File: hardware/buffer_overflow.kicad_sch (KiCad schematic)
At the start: 24 parts, among them J1 Upper Connector, J2 Lower Connector, U1 LM741

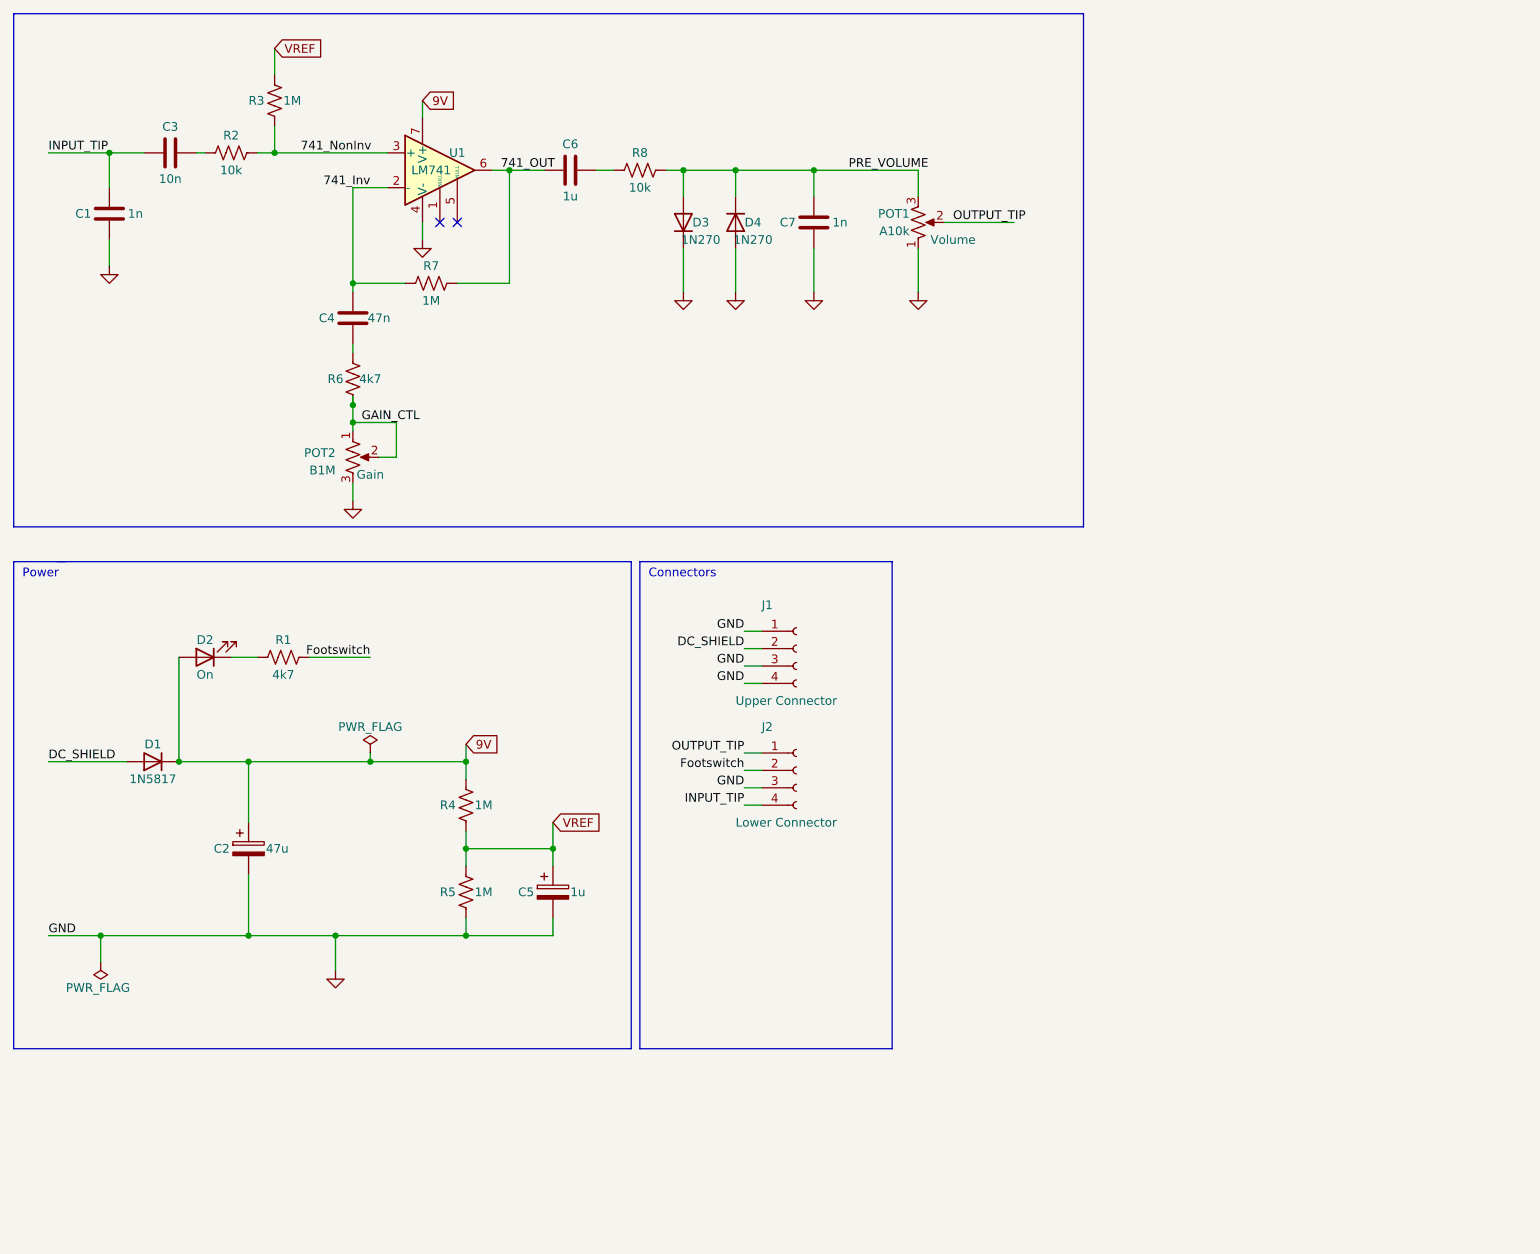
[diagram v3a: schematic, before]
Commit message: Offload functions of "noise floor" interface boards for v0.35
 - more layout changes coming, but functionality should be the same.
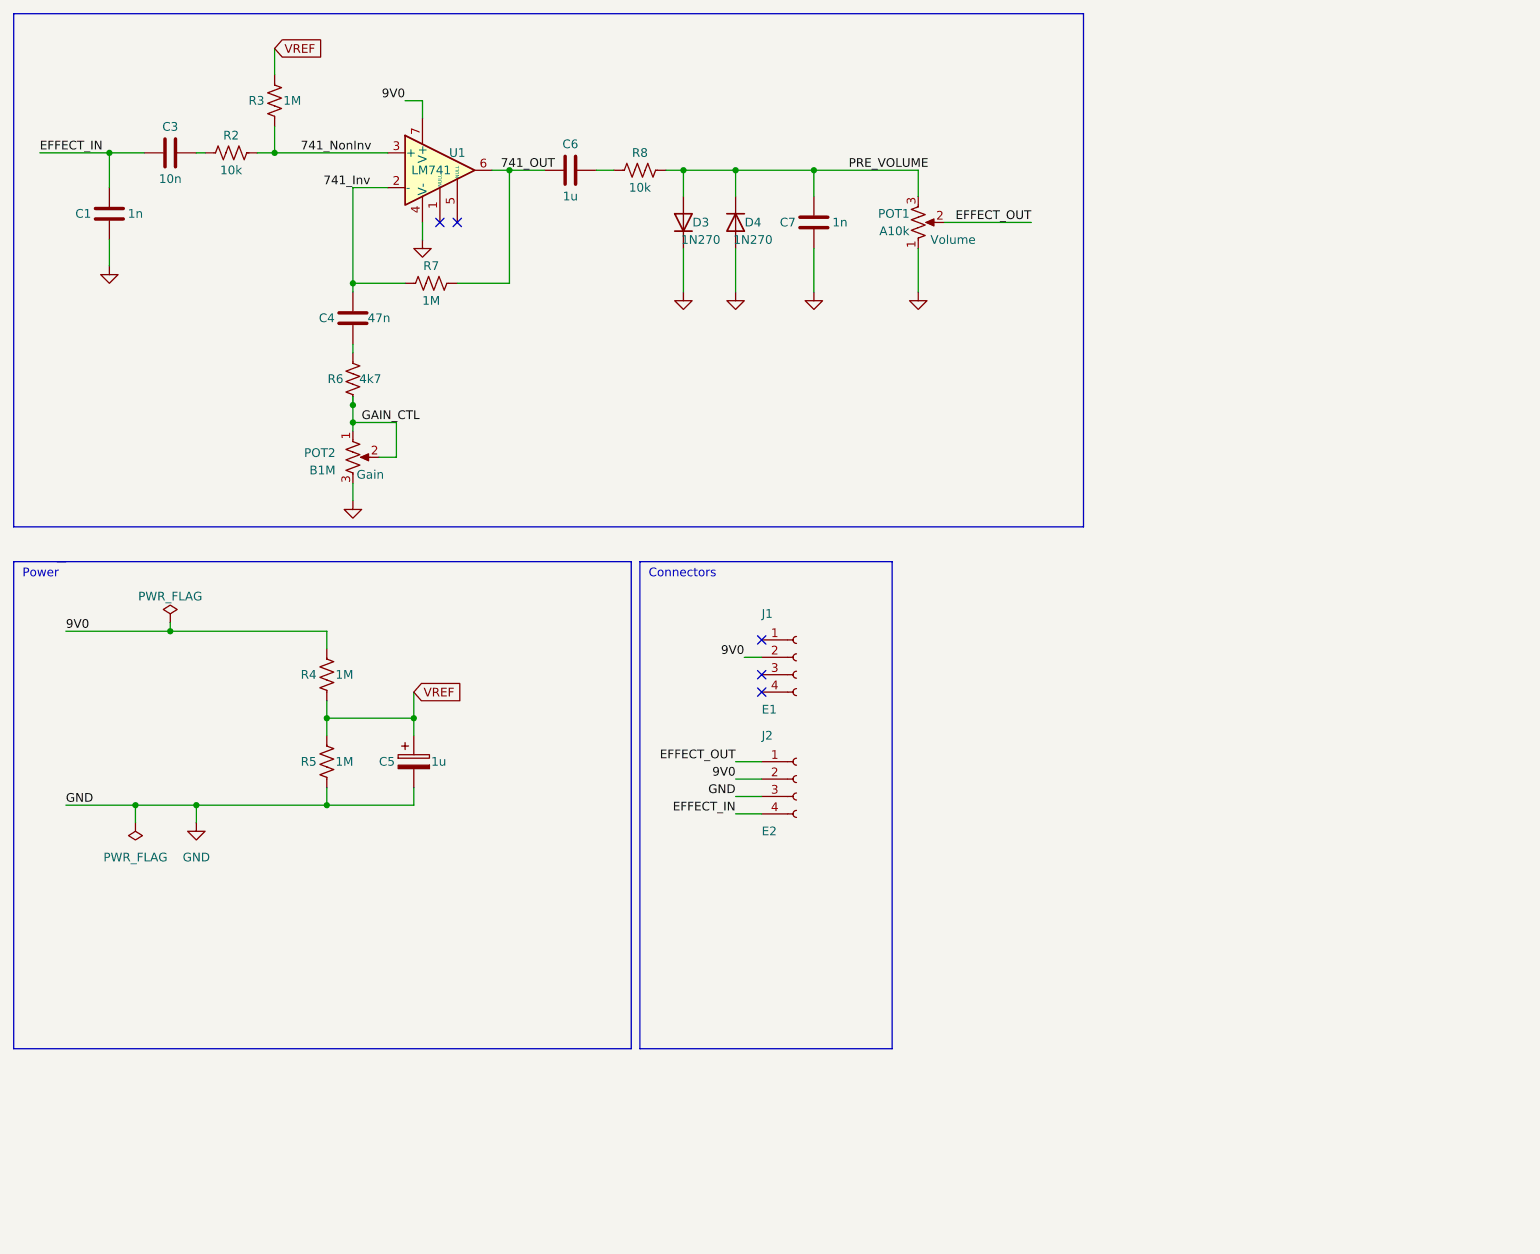
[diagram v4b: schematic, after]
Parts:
- removed C2: 47u, Capacitor_THT:CP_Radial_D5.0mm_P2.50mm, symbol Device:C_Polarized
- removed D1: 1N5817, Diode_THT:D_DO-35_SOD27_P7.62mm_Horizontal, symbol Device:D
- removed D2: On, LED_THT:LED_D3.0mm, symbol Device:LED
- removed R1: 4k7, Resistor_THT:R_Axial_DIN0207_L6.3mm_D2.5mm_P7.62mm_Horizontal, symbol Device:R_US
- J1: value Upper Connector -> E1
- J2: value Lower Connector -> E2
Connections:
- net DC_SHIELD is gone; now on net 9V0: J1.2 (Pin_2)
- net Footswitch is gone; now on net 9V0: J2.2 (Pin_2)
- net GND: no longer J1.1 (Pin_1), J1.3 (Pin_3), J1.4 (Pin_4)
- net 9V renamed 9V0
- net INPUT_TIP renamed EFFECT_IN
- net OUTPUT_TIP renamed EFFECT_OUT
- no-connect marks 2 -> 5
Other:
- moved on the sheet: C5, R4, R5

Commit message: condense to a single connector, bump rev to v0.38
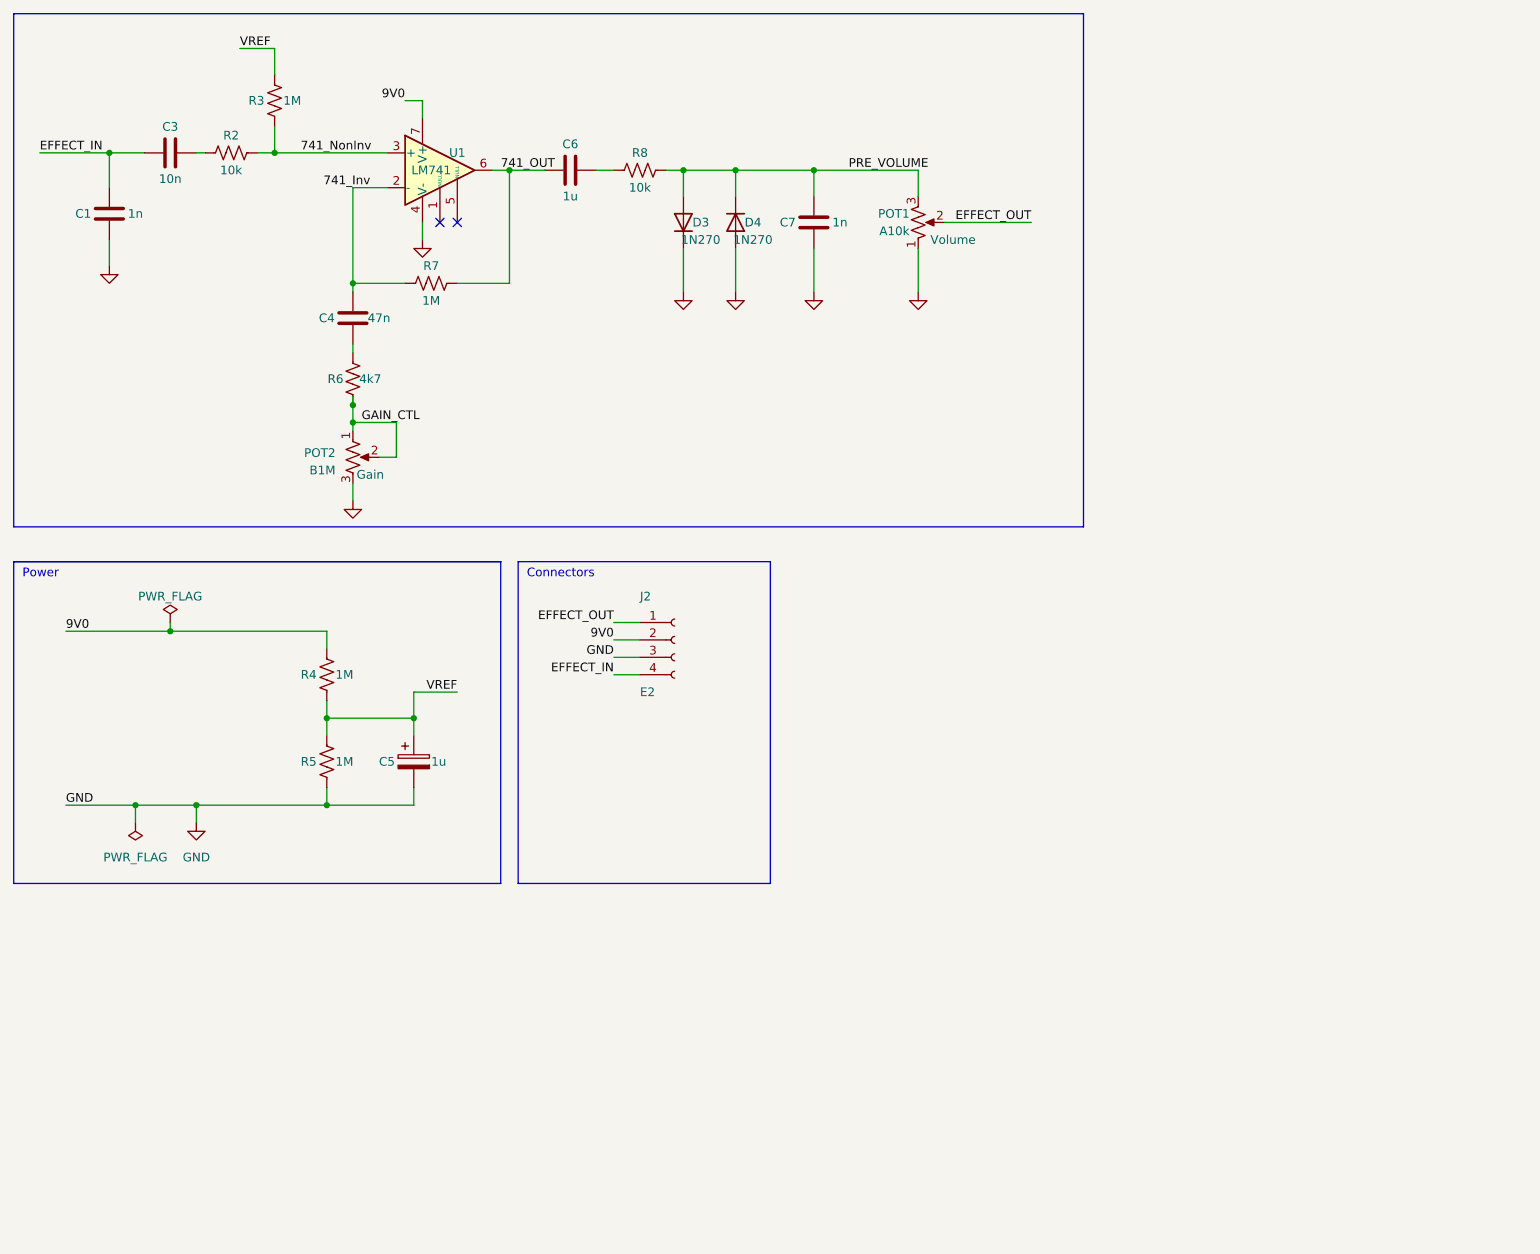
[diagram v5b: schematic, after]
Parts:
- removed J1: E1, Connector_Molex:Molex_PicoBlade_53047-0410_1x04_P1.25mm_Vertical, symbol Connector:Conn_01x04_Socket
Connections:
- no-connect marks 5 -> 2
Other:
- moved on the sheet: J2
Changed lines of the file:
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@@
     (title "Buffer Overflow Drive Effect")
     (date "2023-03-03")
-    (rev "v0.35")
+    (rev "v0.38")
     (company "github.com/whbeers/buffer_overflow")
   )
@@
   (no_connect (at 80.01 45.72))
   (no_connect (at 77.47 45.72))
-  (no_connect (at 124.46 114.3))
-  (no_connect (at 124.46 111.76))
-  (no_connect (at 124.46 106.68))
   (wire (pts (xy 132.08 38.1) (xy 147.32 38.1))
     (stroke (width 0) (type default))
   )
+  (polyline (pts (xy 86.36 142.24) (xy 86.36 95.25))
+    (stroke (width 0) (type default))
+  )
   (wire (pts (xy 64.77 71.12) (xy 64.77 72.39))
     (stroke (width 0) (type default))
   )
-  (wire (pts (xy 120.65 129.54) (xy 124.46 129.54))
+  (wire (pts (xy 102.87 109.22) (xy 106.68 109.22))
     (stroke (width 0) (type default))
   )
@@
     (stroke (width 0) (type default))
   )
-  (polyline (pts (xy 21.59 95.25) (xy 105.41 95.25))
-    (stroke (width 0) (type default))
-  )
   (wire (pts (xy 60.96 107.95) (xy 60.96 105.41))
     (stroke (width 0) (type default))
@@
     (stroke (width 0) (type default))
   )
-  (polyline (pts (xy 106.68 95.25) (xy 106.68 166.37))
+  (polyline (pts (xy 88.9 95.25) (xy 88.9 142.24))
     (stroke (width 0) (type default))
   )
@@
     (stroke (width 0) (type default))
   )
-  (polyline (pts (xy 106.68 166.37) (xy 143.51 166.37))
+  (polyline (pts (xy 88.9 142.24) (xy 125.73 142.24))
     (stroke (width 0) (type default))
   )
@@
     (stroke (width 0) (type default))
   )
-  (wire (pts (xy 121.92 109.22) (xy 124.46 109.22))
-    (stroke (width 0) (type default))
-  )
-  (polyline (pts (xy 105.41 95.25) (xy 105.41 166.37))
-    (stroke (width 0) (type default))
-  )
-  (polyline (pts (xy 15.24 95.25) (xy 15.24 166.37))
+  (polyline (pts (xy 15.24 95.25) (xy 86.36 95.25))
+    (stroke (width 0) (type default))
+  )
+  (polyline (pts (xy 15.24 95.25) (xy 15.24 142.24))
     (stroke (width 0) (type default))
   )
@@
     (stroke (width 0) (type default))
   )
-  (polyline (pts (xy 143.51 166.37) (xy 143.51 95.25))
-    (stroke (width 0) (type default))
-  )
-  (wire (pts (xy 120.65 127) (xy 124.46 127))
+  (polyline (pts (xy 125.73 142.24) (xy 125.73 95.25))
+    (stroke (width 0) (type default))
+  )
+  (wire (pts (xy 102.87 106.68) (xy 106.68 106.68))
     (stroke (width 0) (type default))
   )
@@
     (stroke (width 0) (type default))
   )
+  (polyline (pts (xy 15.24 142.24) (xy 86.36 142.24))
+    (stroke (width 0) (type default))
+  )
   (wire (pts (xy 41.91 35.56) (xy 43.18 35.56))
     (stroke (width 0) (type default))
@@
     (stroke (width 0) (type default))
   )
+  (wire (pts (xy 48.26 20.32) (xy 53.34 20.32))
+    (stroke (width 0) (type default))
+  )
   (wire (pts (xy 68.58 80.01) (xy 71.12 80.01))
     (stroke (width 0) (type default))
@@
     (stroke (width 0) (type default))
   )
-  (wire (pts (xy 120.65 132.08) (xy 124.46 132.08))
+  (wire (pts (xy 102.87 111.76) (xy 106.68 111.76))
     (stroke (width 0) (type default))
   )
@@
     (stroke (width 0) (type default))
   )
-  (polyline (pts (xy 105.41 166.37) (xy 15.24 166.37))
+  (polyline (pts (xy 86.36 95.25) (xy 15.24 95.25))
     (stroke (width 0) (type default))
   )
@@
     (stroke (width 0) (type default))
   )
-  (polyline (pts (xy 15.24 95.25) (xy 22.86 95.25))
-    (stroke (width 0) (type default))
-  )
-  (wire (pts (xy 120.65 124.46) (xy 124.46 124.46))
+  (wire (pts (xy 102.87 104.14) (xy 106.68 104.14))
+    (stroke (width 0) (type default))
+  )
+  (wire (pts (xy 73.66 114.3) (xy 80.01 114.3))
     (stroke (width 0) (type default))
   )
@@
     (stroke (width 0) (type default))
   )
-  (polyline (pts (xy 106.68 95.25) (xy 143.51 95.25))
+  (polyline (pts (xy 88.9 95.25) (xy 125.73 95.25))
     (stroke (width 0) (type default))
   )
@@
     (stroke (width 0) (type default))
   )
-  (text "Connectors" (at 107.95 97.79 0)
+  (text "Connectors" (at 90.17 97.79 0)
     (effects (font (size 1.27 1.27)) (justify left bottom))
   )
@@
     (effects (font (size 1.27 1.27)) (justify right bottom))
   )
-  (label "9V0" (at 121.92 109.22 180) (fields_autoplaced)
-    (effects (font (size 1.27 1.27)) (justify right bottom))
-  )
   (label "EFFECT_IN" (at 19.05 35.56 0) (fields_autoplaced)
     (effects (font (size 1.27 1.27)) (justify left bottom))
@@
     (effects (font (size 1.27 1.27)) (justify left bottom))
   )
+  (label "VREF" (at 48.26 20.32 0) (fields_autoplaced)
+    (effects (font (size 1.27 1.27)) (justify left bottom))
+  )
+  (label "VREF" (at 80.01 114.3 180) (fields_autoplaced)
+    (effects (font (size 1.27 1.27)) (justify right bottom))
+  )
   (label "9V0" (at 22.86 105.41 0) (fields_autoplaced)
     (effects (font (size 1.27 1.27)) (justify left bottom))
   )
-  (label "EFFECT_IN" (at 120.65 132.08 180) (fields_autoplaced)
+  (label "EFFECT_IN" (at 102.87 111.76 180) (fields_autoplaced)
     (effects (font (size 1.27 1.27)) (justify right bottom))
   )
@@
     (effects (font (size 1.27 1.27)) (justify left bottom))
   )
-  (label "EFFECT_OUT" (at 120.65 124.46 180) (fields_autoplaced)
+  (label "EFFECT_OUT" (at 102.87 104.14 180) (fields_autoplaced)
     (effects (font (size 1.27 1.27)) (justify right bottom))
   )
@@
     (effects (font (size 1.27 1.27)) (justify left bottom))
   )
-  (label "9V0" (at 120.65 127 180) (fields_autoplaced)
+  (label "9V0" (at 102.87 106.68 180) (fields_autoplaced)
     (effects (font (size 1.27 1.27)) (justify right bottom))
   )
-  (label "GND" (at 120.65 129.54 180) (fields_autoplaced)
+  (label "GND" (at 102.87 109.22 180) (fields_autoplaced)
     (effects (font (size 1.27 1.27)) (justify right bottom))
-  )
-  (global_label "VREF" (shape input) (at 73.66 114.3 0) (fields_autoplaced)
-    (effects (font (size 1.27 1.27)) (justify left))
-    (property "Intersheetrefs" "${INTERSHEET_REFS}" (at 80.6693 114.2206 0)
-      (effects (font (size 1.27 1.27)) (justify left) hide)
-    )
-  )
-  (global_label "VREF" (shape input) (at 53.34 20.32 0) (fields_autoplaced)
-    (effects (font (size 1.27 1.27)) (justify left))
-    (property "Intersheetrefs" "${INTERSHEET_REFS}" (at 60.3493 20.2406 0)
-      (effects (font (size 1.27 1.27)) (justify left) hide)
-    )
   )
   (symbol (lib_id "Device:R_US") (at 60.96 124.46 180) (unit 1)
@@
         (path "/65eca179-3106-4a88-bde8-4fcb23cd7118"
           (reference "C7") (unit 1)
-        )
-      )
-    )
-  )
-  (symbol (lib_id "Connector:Conn_01x04_Socket") (at 129.54 109.22 0) (unit 1)
-    (in_bom yes) (on_board yes) (dnp no)
-    (property "Reference" "J1" (at 124.46 102.87 0)
-      (effects (font (size 1.27 1.27)) (justify left))
-    )
-    (property "Value" "E1" (at 124.46 116.84 0)
-      (effects (font (size 1.27 1.27)) (justify left))
-    )
-    (property "Footprint" "Connector_Molex:Molex_PicoBlade_53047-0410_1x04_P1.25mm_Vertical" (at 129.54 109.22 0)
-      (effects (font (size 1.27 1.27)) hide)
-    )
-    (property "Datasheet" "~" (at 129.54 109.22 0)
-      (effects (font (size 1.27 1.27)) hide)
-    )
-    (pin "1")
-    (pin "2")
-    (pin "3")
-    (pin "4")
-    (instances
-      (project "random_input"
-        (path "/5002b35c-f20f-46af-a67b-ad193e6bd925"
-          (reference "J1") (unit 1)
-        )
-      )
-      (project "buffer_overflow"
-        (path "/65eca179-3106-4a88-bde8-4fcb23cd7118"
-          (reference "J1") (unit 1)
         )
       )
@@
     )
   )
-  (symbol (lib_id "Connector:Conn_01x04_Socket") (at 129.54 127 0) (unit 1)
-    (in_bom yes) (on_board yes) (dnp no)
-    (property "Reference" "J2" (at 124.46 120.65 0)
+  (symbol (lib_id "Connector:Conn_01x04_Socket") (at 111.76 106.68 0) (unit 1)
+    (in_bom yes) (on_board yes) (dnp no)
+    (property "Reference" "J2" (at 106.68 100.33 0)
       (effects (font (size 1.27 1.27)) (justify left))
     )
-    (property "Value" "E2" (at 124.46 134.62 0)
+    (property "Value" "E2" (at 106.68 114.3 0)
       (effects (font (size 1.27 1.27)) (justify left))
     )
-    (property "Footprint" "Connector_Molex:Molex_PicoBlade_53047-0410_1x04_P1.25mm_Vertical" (at 129.54 127 0)
-      (effects (font (size 1.27 1.27)) hide)
-    )
-    (property "Datasheet" "~" (at 129.54 127 0)
+    (property "Footprint" "Connector_Molex:Molex_PicoBlade_53047-0410_1x04_P1.25mm_Vertical" (at 111.76 106.68 0)
+      (effects (font (size 1.27 1.27)) hide)
+    )
+    (property "Datasheet" "~" (at 111.76 106.68 0)
       (effects (font (size 1.27 1.27)) hide)
     )
@@
       (project "buffer_overflow"
         (path "/65eca179-3106-4a88-bde8-4fcb23cd7118"
-          (reference "J2") (unit 1)
-        )
-      )
+          (reference "J1") (unit 1)
+        )
+      )

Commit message: update schematic with correct identifier for E1
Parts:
- J2: value E2 -> E1
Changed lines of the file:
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@@
       (effects (font (size 1.27 1.27)) (justify left))
     )
-    (property "Value" "E2" (at 106.68 114.3 0)
+    (property "Value" "E1" (at 106.68 114.3 0)
       (effects (font (size 1.27 1.27)) (justify left))
     )
